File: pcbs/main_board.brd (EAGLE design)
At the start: 94 x 20 mm, 36 parts, among them IC1 317T, IC2 MEGA48/88/168-AU, J1 22-27-2021-02, K1 G6K-2F, Q1 MOSFET-NCHANNELSMD, Q2 MOSFET-NCHANNELSMD

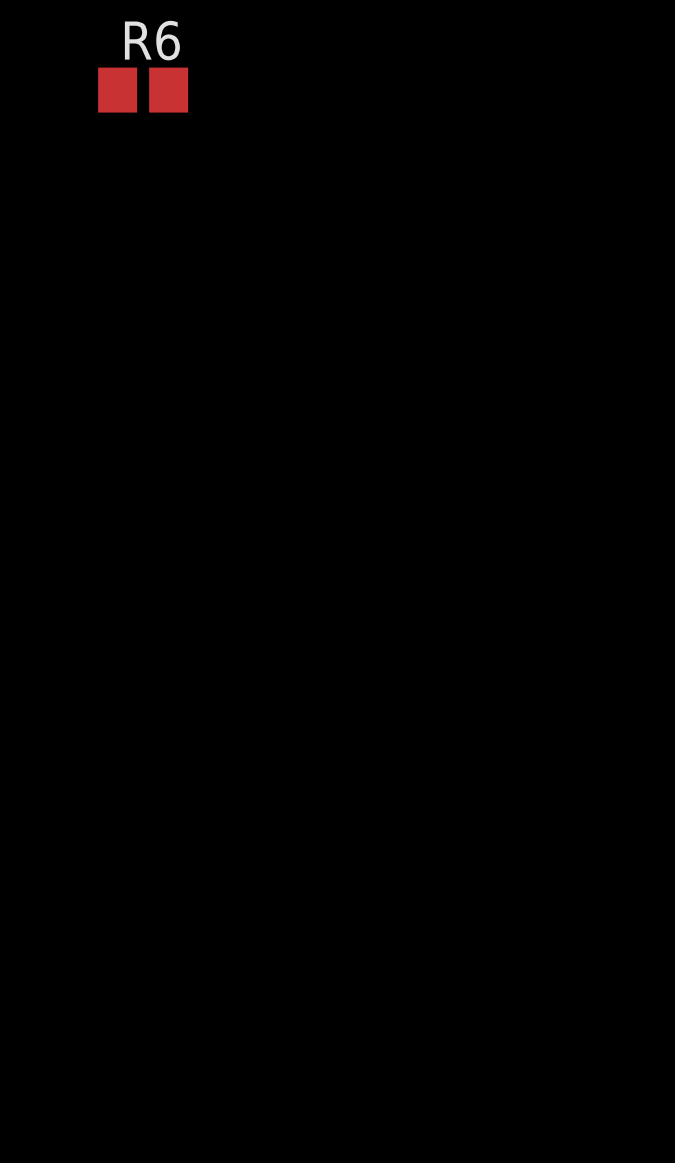
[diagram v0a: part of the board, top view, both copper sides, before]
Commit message: Main Board: Added connections to front and to tail light.
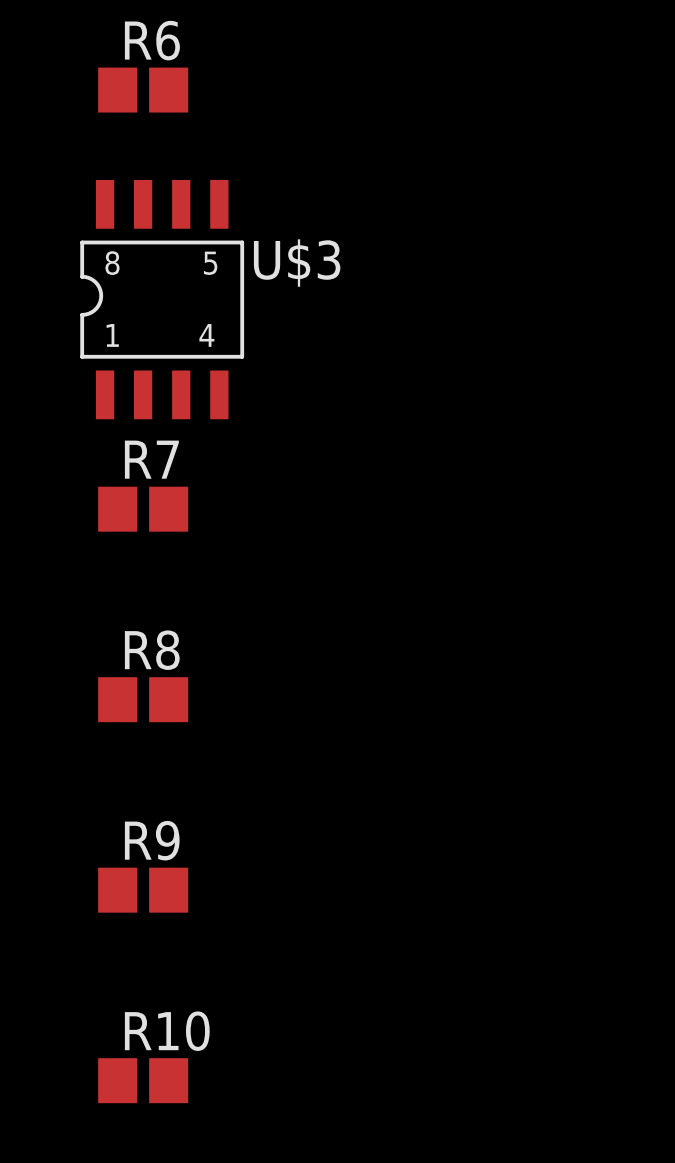
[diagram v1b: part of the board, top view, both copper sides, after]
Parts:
- added R10, R9: 1k, resistor:R0805
- added R7, R8: 100k, resistor:R0805
- added U$3: IRF7103, irf-2:SO8-2
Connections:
- removed net N$11: JP1.3
- removed net N$7: JP1.2
- new net FRONT_POWER: R10.1
- new net FRONT_SCL: IC2.28, JP1.4
- new net FRONT_SDA: IC2.27, JP1.3
- new net N$13: JP1.5, U$3.5, U$3.6
- new net N$18: JP2.3, U$3.7, U$3.8
- new net N$19: R10.2, R7.1, U$3.4
- new net N$20: R8.1, R9.2, U$3.2
- new net N$21: IC2.22
- new net N$22: IC2.26
- new net N$23: IC2.25
- new net N$24: IC2.24
- new net N$25: IC2.23
- new net N$26: IC2.30
- new net N$27: IC2.31
- new net N$28: IC2.32
- new net TAIL_LIGHT: JP2.2
- new net TAIL_POWER: R9.1
- new net TAIL_PWM: JP2.4
- net +12V: now also JP2.1
- net GND: now also R7.2, R8.2, U$3.1, U$3.3; no longer JP1.5
- net N$12: now also IC2.19; no longer JP1.4
- net VCC: now also JP1.2
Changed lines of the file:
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@@
 <element name="R5" library="resistor" package="R0805" value="100k" x="-45.72" y="-100.33"/>
 <element name="R6" library="resistor" package="R0805" value="1k" x="-45.72" y="-106.68"/>
+<element name="U$3" library="irf-2" package="SO8-2" value="IRF7103" x="-44.45" y="-114.3"/>
+<element name="R7" library="resistor" package="R0805" value="100k" x="-45.72" y="-120.65"/>
+<element name="R8" library="resistor" package="R0805" value="100k" x="-45.72" y="-127"/>
+<element name="R9" library="resistor" package="R0805" value="1k" x="-45.72" y="-133.35"/>
+<element name="R10" library="resistor" package="R0805" value="1k" x="-45.72" y="-139.7"/>
 </elements>
 <signals>
@@
 <contactref element="Q1" pad="2"/>
 <contactref element="R2" pad="1"/>
-<contactref element="JP1" pad="5"/>
 <contactref element="JP4" pad="5"/>
 <contactref element="Q2" pad="2"/>
 <contactref element="R5" pad="2"/>
+<contactref element="U$3" pad="1"/>
+<contactref element="U$3" pad="3"/>
+<contactref element="R7" pad="2"/>
+<contactref element="R8" pad="2"/>
+<wire x1="-44.87" y1="-120.65" x2="-44.87" y2="-127" width="0" layer="19" extent="1-1"/>
+<wire x1="-44.45" y1="-116.84" x2="-44.87" y2="-120.65" width="0" layer="19" extent="1-1"/>
+<wire x1="-46.99" y1="-116.84" x2="-44.45" y2="-116.84" width="0" layer="19" extent="1-1"/>
+<wire x1="-44.87" y1="-100.33" x2="-44.45" y2="-116.84" width="0" layer="19" extent="1-1"/>
 <wire x1="-46.04" y1="-94.98" x2="-44.87" y2="-100.33" width="0" layer="19" extent="1-1"/>
-<wire x1="-31.75" y1="-80.01" x2="-46.04" y2="-94.98" width="0" layer="19" extent="1-1"/>
-<wire x1="-31.75" y1="-67.31" x2="-31.75" y2="-80.01" width="0" layer="19" extent="1-1"/>
+<wire x1="-31.75" y1="-67.31" x2="-46.04" y2="-94.98" width="0" layer="19" extent="1-1"/>
 <wire x1="-42.76" y1="-57.15" x2="-31.75" y2="-67.31" width="0" layer="19" extent="1-1"/>
 <wire x1="-42.23" y1="-53.07" x2="-42.76" y2="-57.15" width="0" layer="19" extent="1-1"/>
@@
 <wire x1="3.81" y1="15.24" x2="-22.3774" y2="-4.68" width="0" layer="19" extent="1-1"/>
 <wire x1="12.185" y1="7.62" x2="3.81" y2="15.24" width="0" layer="19" extent="1-1"/>
-<wire x1="12.185" y1="3.81" x2="12.185" y2="7.62" width="0" layer="19" extent="1-1"/>
-<wire x1="25.4" y1="4.74" x2="12.185" y2="3.81" width="0" layer="19" extent="1-1"/>
-<wire x1="36.83" y1="4.74" x2="25.4" y2="4.74" width="0" layer="19" extent="1-1"/>
-<wire x1="46.03" y1="13.97" x2="36.83" y2="4.74" width="0" layer="19" extent="1-1"/>
-<wire x1="66.88" y1="2.54" x2="46.03" y2="13.97" width="0" layer="19" extent="1-1"/>
 </signal>
 <signal name="N$6">
@@
 <contactref element="C9" pad="1"/>
 <contactref element="C11" pad="1"/>
+<contactref element="JP1" pad="2"/>
+<wire x1="-38.23" y1="-31.75" x2="-39.37" y2="-80.01" width="0" layer="19" extent="1-1"/>
 <wire x1="-38.95" y1="-26.67" x2="-38.23" y2="-31.75" width="0" layer="19" extent="1-1"/>
 <wire x1="-38.95" y1="-22.86" x2="-38.95" y2="-26.67" width="0" layer="19" extent="1-1"/>
@@
 <contactref element="U$2" pad="3"/>
 <contactref element="R4" pad="2"/>
+<contactref element="JP2" pad="1"/>
 <wire x1="-40.64" y1="-90.17" x2="-41.06" y2="-93.98" width="0" layer="19" extent="1-1"/>
 <wire x1="-41.91" y1="-90.17" x2="-40.64" y2="-90.17" width="0" layer="19" extent="1-1"/>
 <wire x1="-43.18" y1="-90.17" x2="-41.91" y2="-90.17" width="0" layer="19" extent="1-1"/>
 <wire x1="-41.91" y1="-80.01" x2="-41.91" y2="-90.17" width="0" layer="19" extent="1-1"/>
-<wire x1="-37.15" y1="-13.94" x2="-41.91" y2="-80.01" width="0" layer="19" extent="1-1"/>
+<wire x1="-38.1" y1="-45.72" x2="-41.91" y2="-80.01" width="0" layer="19" extent="1-1"/>
+<wire x1="-37.15" y1="-13.94" x2="-38.1" y2="-45.72" width="0" layer="19" extent="1-1"/>
 <wire x1="1.27" y1="-9.95" x2="-37.15" y2="-13.94" width="0" layer="19" extent="1-1"/>
 <wire x1="77.47" y1="2.54" x2="1.27" y2="-9.95" width="0" layer="19" extent="1-1"/>
@@
 <contactref element="JP5" pad="2"/>
 </signal>
-<signal name="N$7">
-<contactref element="JP1" pad="2"/>
-</signal>
-<signal name="N$11">
+<signal name="FRONT_SDA">
 <contactref element="JP1" pad="3"/>
-</signal>
-<signal name="N$12">
+<contactref element="IC2" pad="27"/>
+<wire x1="-25.47" y1="-0.7874" x2="-36.83" y2="-80.01" width="0" layer="19" extent="1-1"/>
+</signal>
+<signal name="FRONT_SCL">
 <contactref element="JP1" pad="4"/>
+<contactref element="IC2" pad="28"/>
+<wire x1="-26.27" y1="-0.7874" x2="-34.29" y2="-80.01" width="0" layer="19" extent="1-1"/>
 </signal>
 <signal name="CELL_3">
@@
 <contactref element="JP4" pad="2"/>
 </signal>
+<signal name="N$13">
+<contactref element="JP1" pad="5"/>
+<contactref element="U$3" pad="5"/>
+<contactref element="U$3" pad="6"/>
+<wire x1="-44.45" y1="-110.49" x2="-43.18" y2="-110.49" width="0" layer="19" extent="1-1"/>
+<wire x1="-31.75" y1="-80.01" x2="-43.18" y2="-110.49" width="0" layer="19" extent="1-1"/>
+</signal>
+<signal name="N$18">
+<contactref element="U$3" pad="7"/>
+<contactref element="U$3" pad="8"/>
+<contactref element="JP2" pad="3"/>
+<wire x1="-46.99" y1="-110.49" x2="-45.72" y2="-110.49" width="0" layer="19" extent="1-1"/>
+<wire x1="-33.02" y1="-45.72" x2="-45.72" y2="-110.49" width="0" layer="19" extent="1-1"/>
+</signal>
+<signal name="N$19">
+<contactref element="R10" pad="2"/>
+<contactref element="U$3" pad="4"/>
+<contactref element="R7" pad="1"/>
+<wire x1="-46.57" y1="-120.65" x2="-44.87" y2="-139.7" width="0" layer="19" extent="1-1"/>
+<wire x1="-43.18" y1="-116.84" x2="-46.57" y2="-120.65" width="0" layer="19" extent="1-1"/>
+</signal>
+<signal name="N$20">
+<contactref element="R9" pad="2"/>
+<contactref element="U$3" pad="2"/>
+<contactref element="R8" pad="1"/>
+<wire x1="-46.57" y1="-127" x2="-44.87" y2="-133.35" width="0" layer="19" extent="1-1"/>
+<wire x1="-45.72" y1="-116.84" x2="-46.57" y2="-127" width="0" layer="19" extent="1-1"/>
+</signal>
+<signal name="TAIL_POWER">
+<contactref element="R9" pad="1"/>
+</signal>
+<signal name="FRONT_POWER">
+<contactref element="R10" pad="1"/>
+</signal>
+<signal name="TAIL_PWM">
+<contactref element="JP2" pad="4"/>
+</signal>
+<signal name="TAIL_LIGHT">
+<contactref element="JP2" pad="2"/>
+</signal>
+<signal name="N$12">
+<contactref element="IC2" pad="19"/>
+</signal>
+<signal name="N$21">
+<contactref element="IC2" pad="22"/>
+</signal>
+<signal name="N$22">
+<contactref element="IC2" pad="26"/>
+</signal>
+<signal name="N$23">
+<contactref element="IC2" pad="25"/>
+</signal>
+<signal name="N$24">
+<contactref element="IC2" pad="24"/>
+</signal>
+<signal name="N$25">
+<contactref element="IC2" pad="23"/>
+</signal>
+<signal name="N$26">
+<contactref element="IC2" pad="30"/>
+</signal>
+<signal name="N$27">
+<contactref element="IC2" pad="31"/>
+</signal>
+<signal name="N$28">
+<contactref element="IC2" pad="32"/>
+</signal>
 </signals>

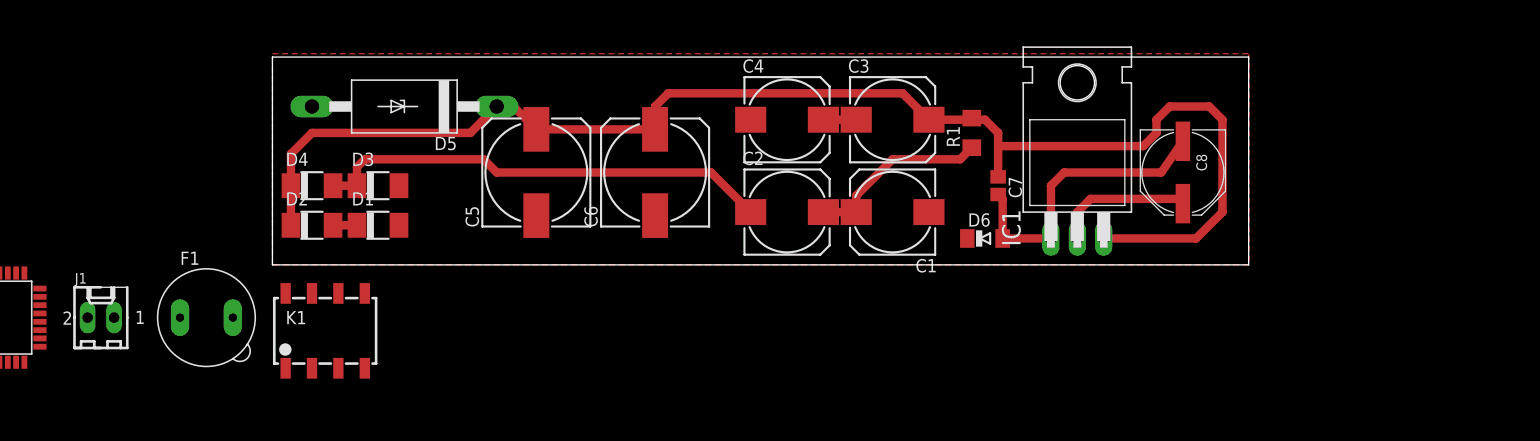
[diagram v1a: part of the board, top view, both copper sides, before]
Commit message: Main Board: Expanded Board to 120 x 20 mm
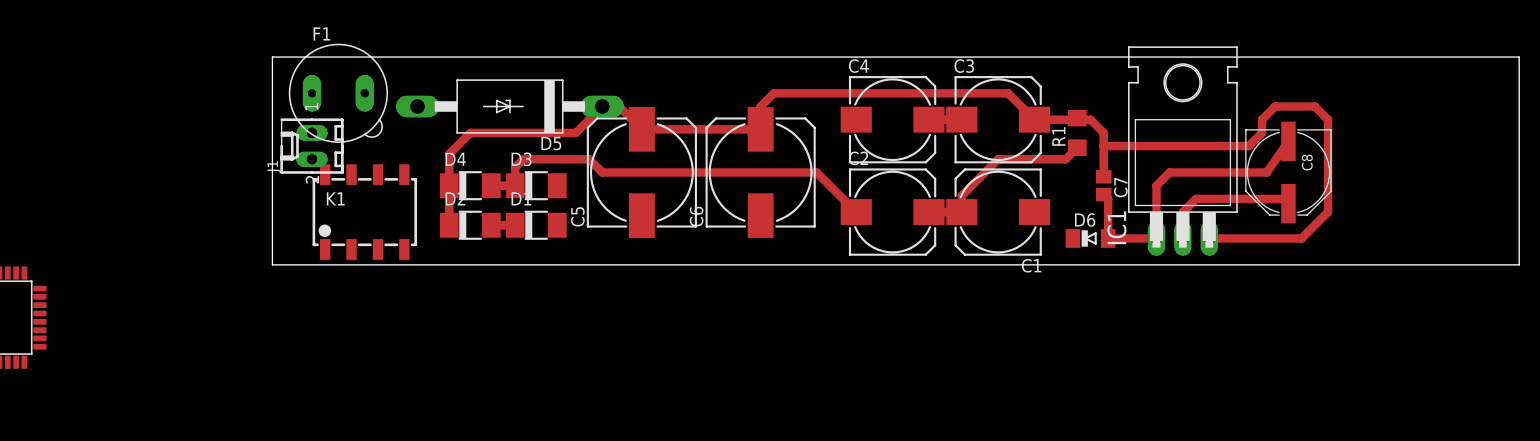
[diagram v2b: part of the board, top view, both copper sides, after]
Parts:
- moved J1 26.2 mm to (3.81, 11.4), turned to 90 degrees
- moved F1 25.0 mm to (6.35, 16.5)
- moved D2 15.2 mm to (19.1, 3.81)
- moved D4 15.2 mm to (19.1, 7.62)
- moved D1 15.2 mm to (25.4, 3.81)
- moved D3 15.2 mm to (25.4, 7.62)
- moved K1 12.0 mm to (8.89, 5.08)
- moved C7 10.2 mm to (80.0, 7.62)
- moved C8 10.2 mm to (97.8, 8.89)
- moved C5 10.2 mm to (35.6, 8.89)
- moved C6 10.2 mm to (47.0, 8.89)
- moved D5 10.2 mm to (22.9, 15.2)
- moved C1 10.2 mm to (69.8, 5.08)
- moved C2 10.2 mm to (59.7, 5.08)
- moved C3 10.2 mm to (69.8, 14.0)
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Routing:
- net N$5: track 132.3 -> 127.2 mm
- net N$2: track 44.4 -> 39.3 mm
- removed copper zone on layer 1, net GND
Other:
- board size 94 x 20 mm -> 120 x 20 mm

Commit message: Main Board: Changed fuse and corrected wrong connection.
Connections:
- removed net N$21: IC2.22
- net TAIL_LIGHT: now also IC2.22
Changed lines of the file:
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@@
 <signal name="TAIL_LIGHT">
 <contactref element="JP2" pad="2"/>
+<contactref element="IC2" pad="22"/>
+<wire x1="-22.3774" y1="-3.88" x2="-35.56" y2="-45.72" width="0" layer="19" extent="1-1"/>
 </signal>
 <signal name="N$12">
 <contactref element="IC2" pad="19"/>
 </signal>
-<signal name="N$21">
-<contactref element="IC2" pad="22"/>
-</signal>
 <signal name="N$22">
